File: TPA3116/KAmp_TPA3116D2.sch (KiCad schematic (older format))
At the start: 87 parts, among them J1 CTRL, J2 R_IN, J3 L_IN, J4 Sync, J5 Sync, J6 R_OUT, J7 Barrel_Jack_Switch, J8 L_OUT, U1 TPA3116D2

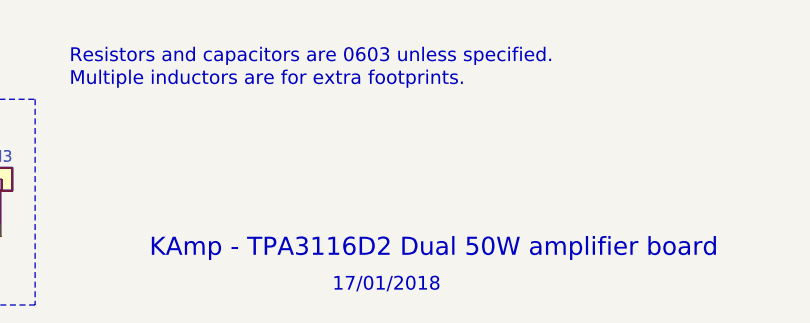
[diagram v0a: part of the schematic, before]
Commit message: 将端子向板边延伸2mm
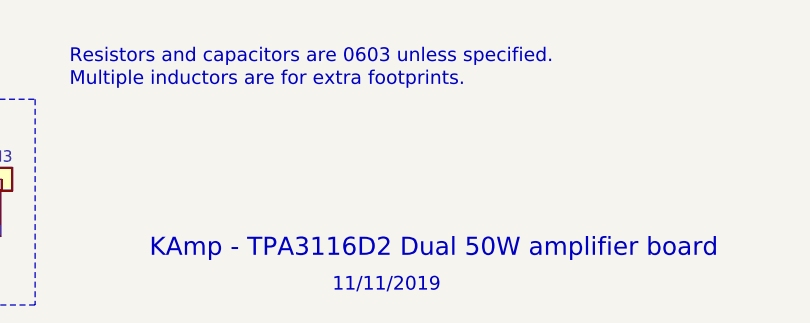
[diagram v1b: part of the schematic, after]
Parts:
- J1: footprint Connector_PinHeader_2.54mm:PinHeader_1x04_P2.54mm_Vertical -> Connector_Molex:Molex_KK-254_AE-6410-04A_1x04_P2.54mm_Vertical
- J2, J3, J4, J5: footprint Connector_PinHeader_2.54mm:PinHeader_1x02_P2.54mm_Vertical -> Connector_Molex:Molex_KK-254_AE-6410-02A_1x02_P2.54mm_Vertical
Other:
- note added: "11/11/2019"
- note removed: "17/01/2018"
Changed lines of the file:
@@
 F 0 "J2" H 1100 2600 50  0000 C CNN
 F 1 "R_IN" V 1200 2450 50  0000 C CNN
-F 2 "Connector_PinHeader_2.54mm:PinHeader_1x02_P2.54mm_Vertical" H 1100 2450 50  0001 C CNN
+F 2 "Connector_Molex:Molex_KK-254_AE-6410-02A_1x02_P2.54mm_Vertical" H 1100 2450 50  0001 C CNN
 F 3 "~" H 1100 2450 50  0001 C CNN
 	1    1100 2450
@@
 F 0 "J3" H 1100 4800 50  0000 C CNN
 F 1 "L_IN" V 1200 4650 50  0000 C CNN
-F 2 "Connector_PinHeader_2.54mm:PinHeader_1x02_P2.54mm_Vertical" H 1100 4650 50  0001 C CNN
+F 2 "Connector_Molex:Molex_KK-254_AE-6410-02A_1x02_P2.54mm_Vertical" H 1100 4650 50  0001 C CNN
 F 3 "~" H 1100 4650 50  0001 C CNN
 	1    1100 4650
@@
 F 0 "J4" H 1100 7150 50  0000 C CNN
 F 1 "Sync" V 1200 7000 50  0000 C CNN
-F 2 "Connector_PinHeader_2.54mm:PinHeader_1x02_P2.54mm_Vertical" H 1100 7000 50  0001 C CNN
+F 2 "Connector_Molex:Molex_KK-254_AE-6410-02A_1x02_P2.54mm_Vertical" H 1100 7000 50  0001 C CNN
 F 3 "~" H 1100 7000 50  0001 C CNN
 	1    1100 7000
@@
 F 0 "J5" H 1100 7500 50  0000 C CNN
 F 1 "Sync" V 1200 7350 50  0000 C CNN
-F 2 "Connector_PinHeader_2.54mm:PinHeader_1x02_P2.54mm_Vertical" H 1100 7350 50  0001 C CNN
+F 2 "Connector_Molex:Molex_KK-254_AE-6410-02A_1x02_P2.54mm_Vertical" H 1100 7350 50  0001 C CNN
 F 3 "~" H 1100 7350 50  0001 C CNN
 	1    1100 7350
@@
 F 0 "J1" H 1100 1450 50  0000 C CNN
 F 1 "CTRL" V 1200 1200 50  0000 C CNN
-F 2 "Connector_PinHeader_2.54mm:PinHeader_1x04_P2.54mm_Vertical" H 1100 1200 50  0001 C CNN
+F 2 "Connector_Molex:Molex_KK-254_AE-6410-04A_1x04_P2.54mm_Vertical" H 1100 1200 50  0001 C CNN
 F 3 "~" H 1100 1200 50  0001 C CNN
 	1    1100 1200
@@
 KAmp - TPA3116D2 Dual 50W amplifier board
 Text Notes 8150 7650 0    60   ~ 0
-17/01/2018
+11/11/2019
 Text Notes 10600 7650 0    60   ~ 0
 001
